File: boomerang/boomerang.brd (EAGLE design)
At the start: 34.3 x 31.8 mm, 11 parts, among them IC1 WS2811-SOP8

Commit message: nicer :)
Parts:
- removed JP1: (no value), adafruit:2X04
- removed PAD1, PAD2, PAD3, PAD4, PAD5, PAD6: (no value), wirepad:SMD1,27-2,54
- added BGND, BO, GGND, GO, RGND, RO: (no value), wirepad:SMD1,27-2,54
- added X3: 87438-06, con-molex:87438-06
- moved Q3 61.2 mm to (-4.76, 8.57), turned to 30 degrees
- moved Q2 54.0 mm to (8.89, 0.00), turned to 270 degrees
- moved IC1 53.4 mm to (3.17, 0.00), turned to 180 degrees
- moved Q1 52.8 mm to (-5.08, -8.57), turned to 150 degrees
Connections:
- net N$1 renamed R
- net N$2 renamed G
- net N$3 renamed B
- removed net N$10: IC1.5, JP1.8
- removed net N$5: IC1.6, JP1.7
- removed net N$6: PAD2.1, Q2.2
- removed net N$7: PAD1.1, Q1.2
- removed net N$9: PAD3.1, Q3.2
- new net BO: BO.1, Q3.2
- new net DIN: IC1.6, X3.3
- new net DO: IC1.5, X3.4
- new net GO: GO.1, Q2.2
- new net RO: Q1.2, RO.1
- net 3V3: now also X3.1; no longer JP1.5, JP1.6
- net GND: now also BGND.1, GGND.1, RGND.1, X3.5, X3.6; no longer JP1.3, JP1.4, PAD4.1, PAD5.1, PAD6.1
- net VCC: now also X3.2; no longer JP1.1, JP1.2
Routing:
- net 3V3: track 99.2 -> 49.7 mm, vias 0 -> 3
- net R: track 8.06 -> 19.4 mm
- net GND: track 2.68 -> 12.6 mm, vias 7 -> 2
- net N$10: track 8.84 -> 0.00 mm
- net DIN: track 0.00 -> 8.70 mm
- net N$5: track 7.94 -> 0.00 mm
- net DO: track 0.00 -> 6.81 mm
- net G: track 15.4 -> 9.37 mm
- net N$6: track 5.20 -> 0.00 mm
- net N$9: track 4.73 -> 0.00 mm
- net BO: track 0.00 -> 3.83 mm
- net GO: track 0.00 -> 3.49 mm
- net RO: track 0.00 -> 3.41 mm
- net B: track 14.1 -> 10.7 mm
- net N$7: track 1.59 -> 0.00 mm
- removed copper zone on layer 16, net GND
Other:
- board size 34.3 x 31.8 mm -> 54.1 x 59.6 mm

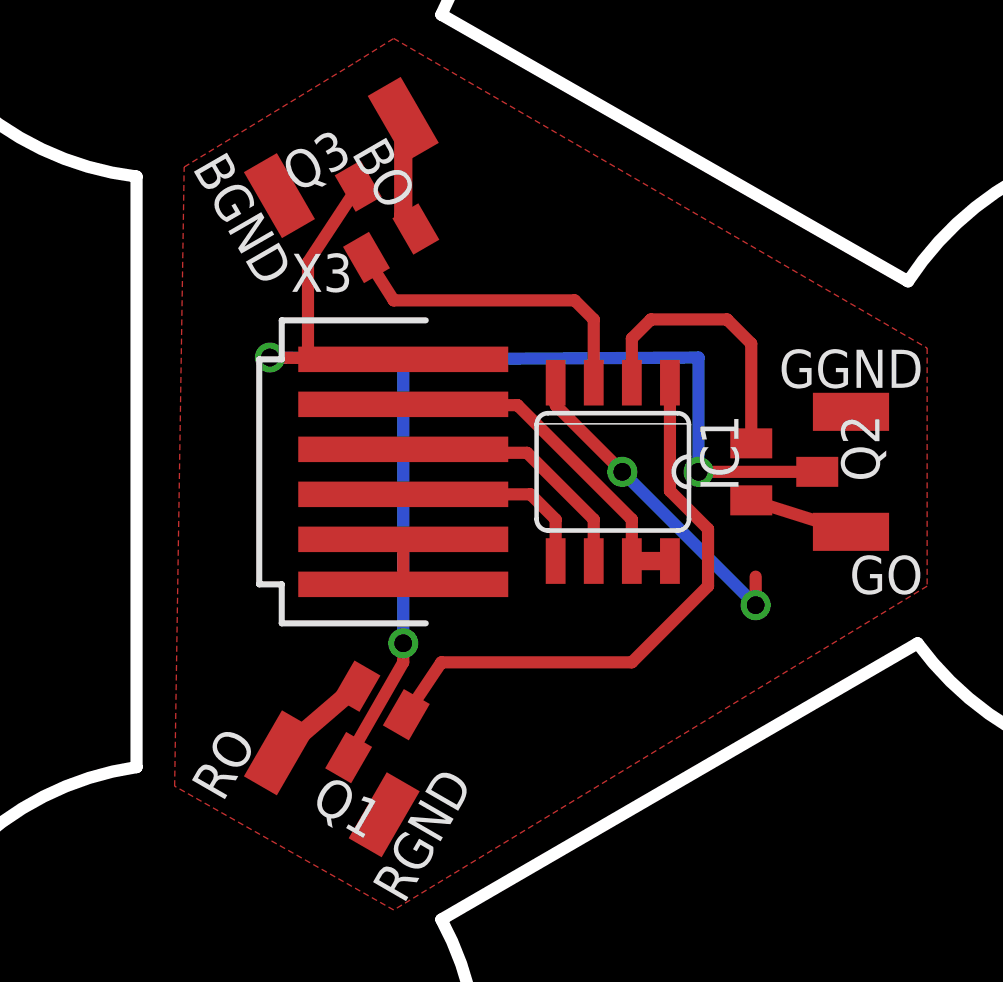
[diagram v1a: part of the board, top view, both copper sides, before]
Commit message: one layer in time
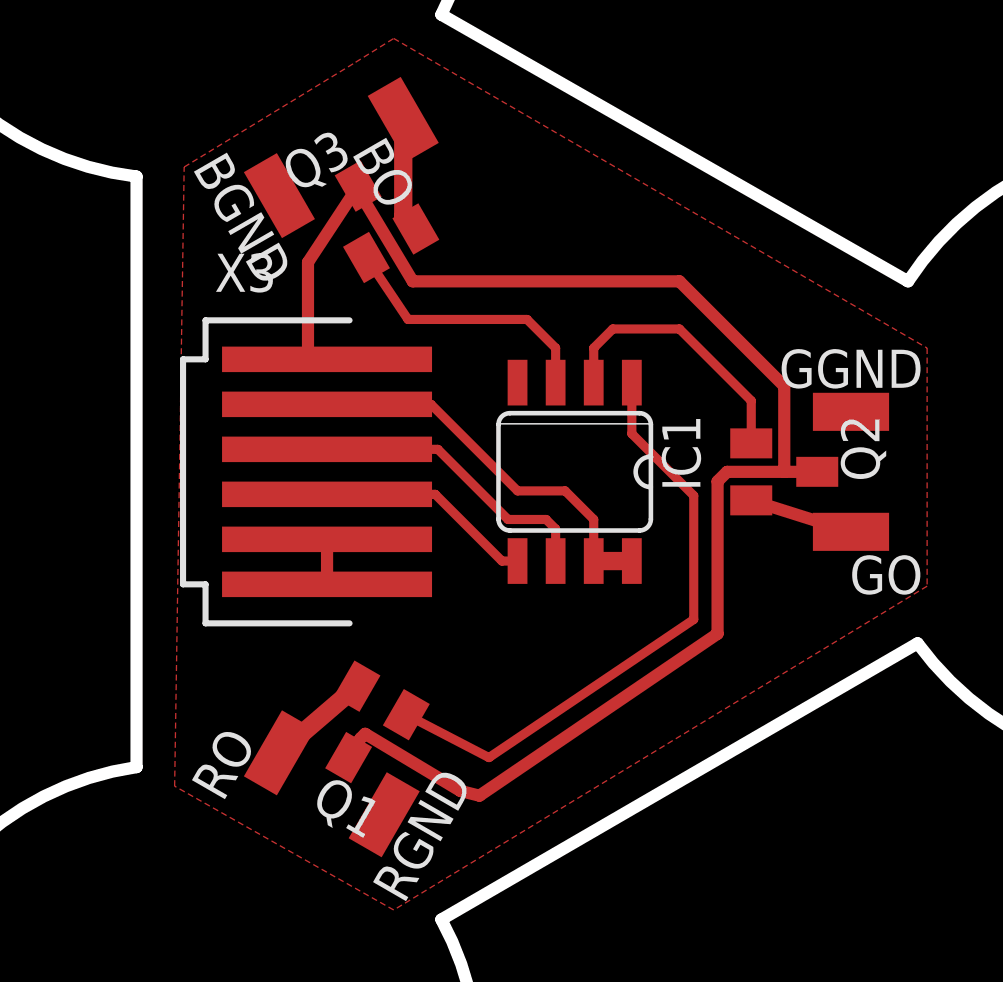
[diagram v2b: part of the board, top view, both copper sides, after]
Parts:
- moved X3 2.54 mm to (-6.35, 0.00)
- moved IC1 1.27 mm to (1.91, 0.00)
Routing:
- net GND: track 12.6 -> 1.50 mm, vias 2 -> 0
- net 3V3: track 49.7 -> 55.7 mm, vias 3 -> 0
- net B: track 10.7 -> 8.96 mm
- net VCC: track 11.9 -> 13.1 mm
- net DIN: track 8.70 -> 9.79 mm
- net R: track 19.4 -> 20.1 mm

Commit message: OCD for everyone
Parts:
- moved BGND 0.32 mm to (-7.94, 9.53)
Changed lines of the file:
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@@
 <element name="RGND" library="wirepad" package="SMD1,27-2,54" value="" x="-4.445" y="-11.43" rot="R150"/>
 <element name="GGND" library="wirepad" package="SMD1,27-2,54" value="" x="11.115" y="2" rot="R270"/>
-<element name="BGND" library="wirepad" package="SMD1,27-2,54" value="" x="-7.9375" y="9.2075" rot="R30"/>
+<element name="BGND" library="wirepad" package="SMD1,27-2,54" value="" x="-7.9375" y="9.525" rot="R30"/>
 <element name="Q1" library="adafruit" package="SOT23" value="" x="-5.08" y="-8.5725" rot="R150"/>
 <element name="Q2" library="adafruit" package="SOT23" value="" x="8.89" y="0" rot="R270"/>
@@
 <contactref element="X3" pad="6"/>
 <wire x1="-6.35" y1="-2.25" x2="-6.35" y2="-3.75" width="0.4064" layer="1"/>
-<polygon width="0.6096" layer="1">
+<polygon width="0.6096" layer="1" isolate="0.4064" orphans="yes">
 <vertex x="-4.1275" y="14.44625"/>
 <vertex x="13.6525" y="4.1275"/>
@@
 <contactref element="Q3" pad="3"/>
 <contactref element="X3" pad="1"/>
-<wire x1="-5.3125" y1="9.525125" x2="-6.985" y2="6.985" width="0.4064" layer="1"/>
-<wire x1="-6.985" y1="6.985" x2="-6.985" y2="3.81" width="0.4064" layer="1"/>
+<wire x1="-6.985" y1="7.62" x2="-6.985" y2="3.81" width="0.4064" layer="1"/>
 <wire x1="-6.985" y1="3.81" x2="-3.87" y2="3.81" width="0.4064" layer="1"/>
 <wire x1="-3.87" y1="3.81" x2="-6.35" y2="3.75" width="0.4064" layer="1"/>
@@
 <wire x1="8.89" y1="0" x2="6.985" y2="0" width="0.4064" layer="1"/>
 <wire x1="6.985" y1="0" x2="6.6675" y2="-0.3175" width="0.4064" layer="1"/>
-<wire x1="-5.3975" y1="9.525" x2="-3.4925" y2="6.35" width="0.4064" layer="1"/>
+<wire x1="-5.3975" y1="9.525" x2="-4.977278125" y2="8.82463125" width="0.4064" layer="1"/>
+<wire x1="-4.977278125" y1="8.82463125" x2="-3.4925" y2="6.35" width="0.4064" layer="1"/>
 <wire x1="-3.4925" y1="6.35" x2="5.3975" y2="6.35" width="0.4064" layer="1"/>
 <wire x1="5.3975" y1="6.35" x2="8.89" y2="2.8575" width="0.4064" layer="1"/>
@@
 <wire x1="-5.08" y1="-8.73125" x2="-1.905" y2="-10.63625" width="0.4064" layer="1"/>
 <wire x1="-1.905" y1="-10.63625" x2="-1.27" y2="-10.795" width="0.4064" layer="1"/>
+<wire x1="-6.985" y1="7.62" x2="-4.977278125" y2="8.82463125" width="0.4064" layer="1"/>
 <wire x1="-5.3975" y1="9.525" x2="-5.3125" y2="9.525125" width="0" layer="19" extent="1-1"/>
 </signal>

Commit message: foo
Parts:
- moved Q1 12.9 mm to (5.71, -1.59), turned to 0 degrees
- moved Q2 4.49 mm to (5.71, 3.17), turned to 0 degrees
- moved Q3 3.39 mm to (-1.43, 7.94), turned to 90 degrees
- moved IC1 2.36 mm to (0.32, 1.75)
- moved BO 1.59 mm to (-5.08, 12.7), turned to 90 degrees
- moved BGND 1.59 mm to (-9.21, 10.5), turned to 180 degrees
- moved RO 1.37 mm to (-9.05, -10.2), turned to 0 degrees
- moved RGND 0.90 mm to (-5.08, -12.1), turned to 90 degrees
- moved X3 0.32 mm to (-6.67, 0.00)
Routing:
- net GND: track 1.50 -> 87.2 mm
- net 3V3: track 55.6 -> 22.2 mm
- net RO: track 3.41 -> 19.7 mm
- net R: track 20.1 -> 8.46 mm
- net B: track 8.96 -> 2.27 mm
- net GO: track 3.49 -> 7.35 mm
- net BO: track 3.83 -> 7.46 mm
- net VCC: track 13.1 -> 11.0 mm
- net DIN: track 9.79 -> 7.70 mm
- net DO: track 7.27 -> 5.56 mm
- net G: track 9.08 -> 8.34 mm

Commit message: foo
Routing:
- net BO: track 7.46 -> 6.72 mm
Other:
- board text added: "B+"
- board text added: "B-"
- board text added: "G+"
- board text added: "G-"
- board text added: "R+"
- board text added: "R-"
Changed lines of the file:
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@@
 <dimension x1="-23.1775" y1="-30.7975" x2="33.02" y2="-31.115" x3="5.33175" y3="41.70229375" textsize="1.778" layer="1"/>
 <dimension x1="32.7025" y1="31.115" x2="33.02" y2="-33.02" x3="-29.64385" y3="-1.26193125" textsize="1.778" layer="1"/>
+<text x="13.97" y="0.635" size="1.778" layer="1" font="vector" ratio="20">G-</text>
+<text x="13.97" y="-2.2225" size="1.778" layer="1" font="vector" ratio="20">G+</text>
+<text x="-8.89" y="13.6525" size="1.778" layer="1" font="vector" ratio="20" rot="R135">B-</text>
+<text x="-9.8425" y="16.8275" size="1.778" layer="1" font="vector" ratio="20" rot="R315">B+</text>
+<text x="-11.43" y="-16.1925" size="1.778" layer="1" font="vector" ratio="20" rot="R45">R+</text>
+<text x="-7.62" y="-14.9225" size="1.778" layer="1" font="vector" ratio="20" rot="R225">R-</text>
 </plain>
 <attributes>
@@
 <wire x1="-1.905" y1="-7.9375" x2="-5.08" y2="-11.1125" width="0.4064" layer="1"/>
 <wire x1="-5.08" y1="-11.1125" x2="-5.08" y2="-12.065" width="0.4064" layer="1"/>
-<polygon width="0.4064" layer="1">
+<polygon width="0.4064" layer="1" isolate="0.6096">
 <vertex x="-19.05" y="-39.37"/>
 <vertex x="49.53" y="1.5875"/>
@@
 <contactref element="Q3" pad="2"/>
 <contactref element="BO" pad="1"/>
-<wire x1="-5.08" y1="12.7" x2="-2.2225" y2="12.7" width="0.4064" layer="1"/>
-<wire x1="-2.2225" y1="12.7" x2="-0.3175" y2="10.795" width="0.4064" layer="1"/>
-<wire x1="-0.3175" y1="10.795" x2="-0.3175" y2="8.89875" width="0.4064" layer="1"/>
+<wire x1="-5.08" y1="12.7" x2="-3.4925" y2="12.7" width="0.4064" layer="1"/>
+<wire x1="-3.4925" y1="12.7" x2="-0.3175" y2="9.525" width="0.4064" layer="1"/>
+<wire x1="-0.3175" y1="9.525" x2="-0.3175" y2="8.89875" width="0.4064" layer="1"/>
 <wire x1="-0.3175" y1="8.89875" x2="-0.32875" y2="8.8875" width="0.4064" layer="1"/>
 </signal>
